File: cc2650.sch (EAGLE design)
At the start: 23 parts, among them IC1 TPS73133DBVR, IC4 CC2650MODAMOHR, SW1 SPST_TACT-KMR2, SW3 SPST_TACT-KMR2

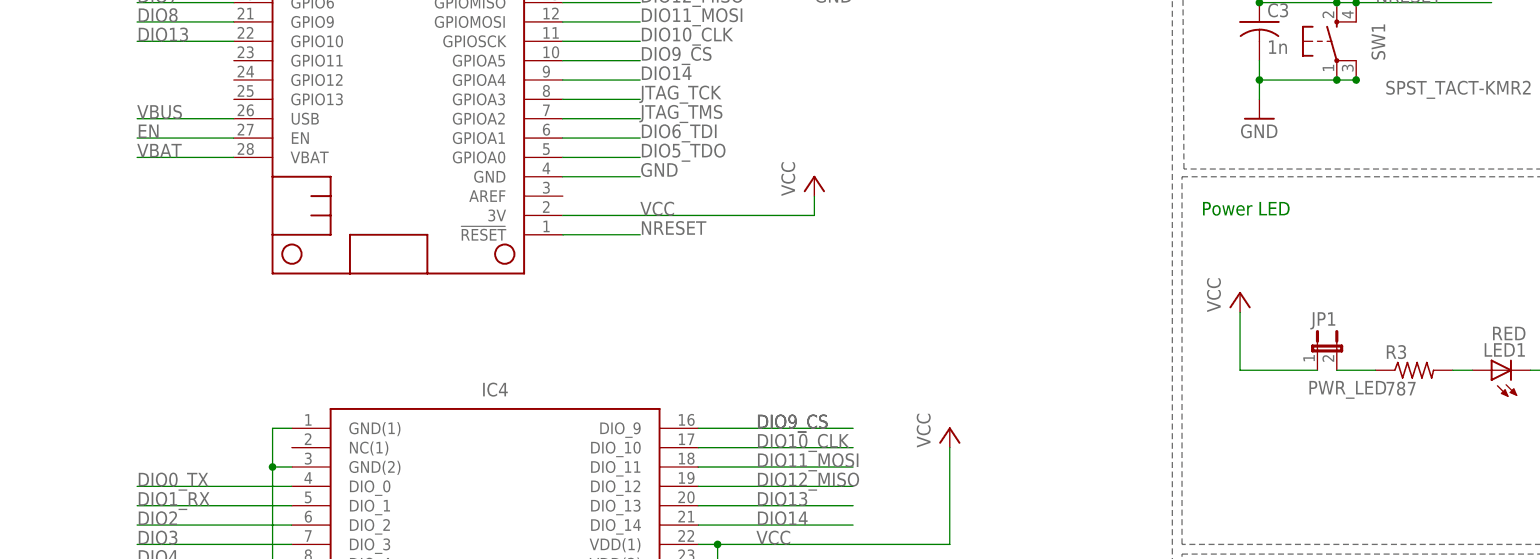
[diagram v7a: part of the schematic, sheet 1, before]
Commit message: routed everything but light sensor
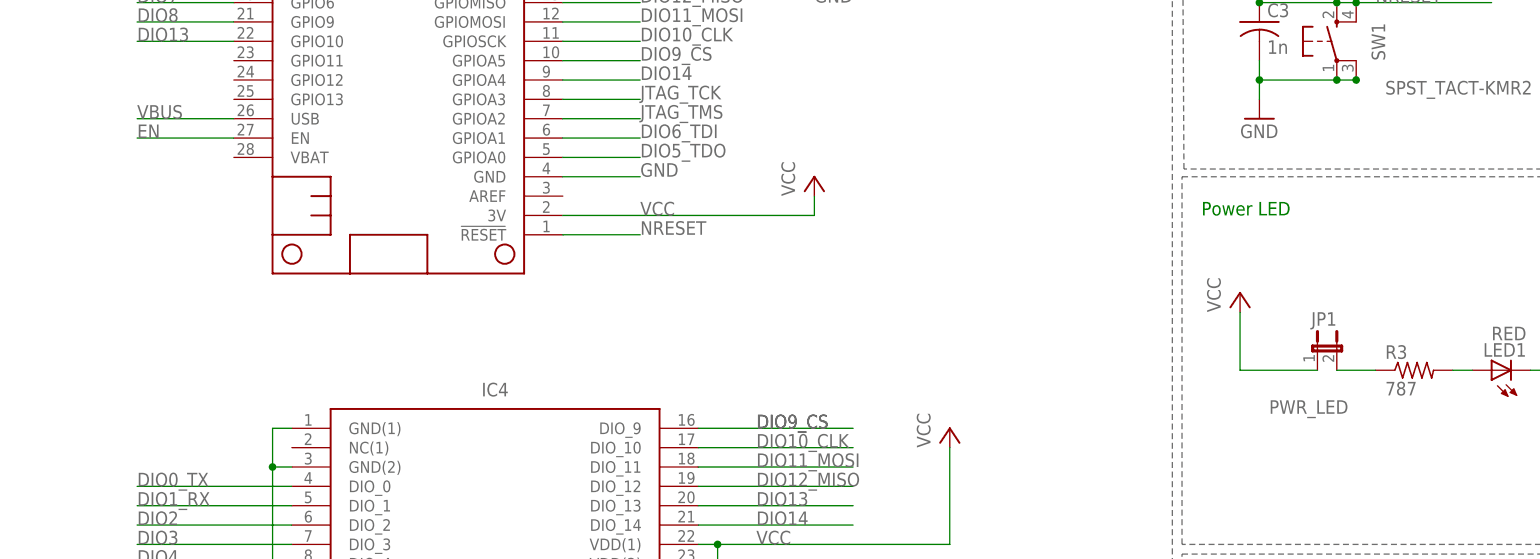
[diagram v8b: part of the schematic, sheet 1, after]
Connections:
- net N$1 renamed PWR_LED_JPR
- net N$2 renamed GPIO_LED
- net N$3 renamed GPIO_LED_JPR
- net N$32 renamed PWR_LED
- net N$5 renamed VCC_JPR
- removed net VBAT: MS1.VBAT
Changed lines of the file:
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@@
 <instance part="JP1" gate="G$1" x="30.48" y="17.78" smashed="yes">
 <attribute name="NAME" x="33.02" y="22.86" size="1.778" layer="95" rot="R180"/>
-<attribute name="VALUE" x="29.21" y="12.065" size="1.778" layer="96"/>
+<attribute name="VALUE" x="24.13" y="9.525" size="1.778" layer="96"/>
 <attribute name="OC_NEWARK" x="30.48" y="17.78" size="1.778" layer="96" display="off"/>
 <attribute name="MF" x="30.48" y="17.78" size="1.778" layer="96" display="off"/>
@@
 </segment>
 </net>
-<net name="N$32" class="0">
+<net name="PWR_LED" class="0">
 <segment>
 <wire x1="50.8" y1="15.24" x2="48.26" y2="15.24" width="0.1524" layer="91"/>
@@
 <label x="144.78" y="-35.56" size="1.778" layer="95"/>
 <pinref part="JP3" gate="G$1" pin="2"/>
-</segment>
-</net>
-<net name="VBAT" class="0">
-<segment>
-<pinref part="MS1" gate="G$1" pin="VBAT"/>
-<wire x1="-111.76" y1="43.18" x2="-124.46" y2="43.18" width="0.1524" layer="91"/>
-<label x="-124.46" y="43.18" size="1.778" layer="95"/>
 </segment>
 </net>
@@
 </segment>
 </net>
-<net name="N$1" class="0">
+<net name="PWR_LED_JPR" class="0">
 <segment>
 <pinref part="R3" gate="G$1" pin="1"/>
@@
 </segment>
 </net>
-<net name="N$5" class="0">
+<net name="VCC_JPR" class="0">
 <segment>
 <pinref part="IC1" gate="G$1" pin="OUT"/>
@@
 </segment>
 </net>
-<net name="N$2" class="0">
+<net name="GPIO_LED" class="0">
 <segment>
 <wire x1="83.82" y1="10.16" x2="81.28" y2="10.16" width="0.1524" layer="91"/>
@@
 </segment>
 </net>
-<net name="N$3" class="0">
+<net name="GPIO_LED_JPR" class="0">
 <segment>
 <pinref part="R2" gate="G$1" pin="1"/>
